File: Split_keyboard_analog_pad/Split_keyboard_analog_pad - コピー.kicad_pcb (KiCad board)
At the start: 2 copper layers, 313.3 x 128.7 mm, 162 parts, among them J1 Conn_01x05_Pin, J2 Conn_01x05_Pin, J3 Conn_01x08_Pin, J4 Conn_01x08_Pin, J5 Conn_01x02, J6 Conn_01x02, M2 MountingHole_2.2mm_M2, U1 nice_nano, U2 nice_nano

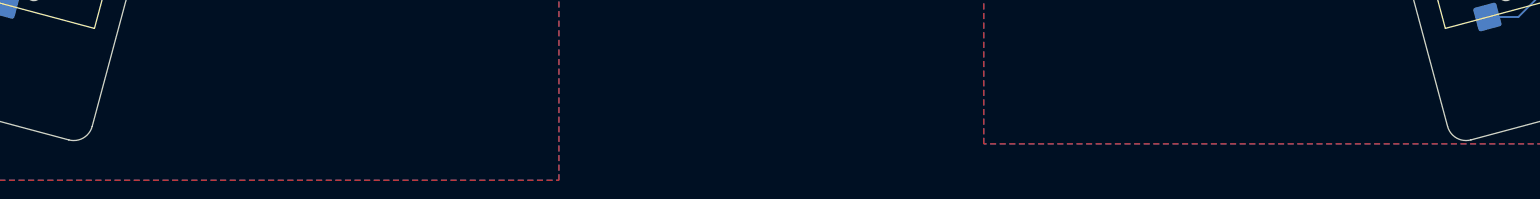
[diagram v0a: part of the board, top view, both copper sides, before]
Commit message: Add BT profile select hold tap
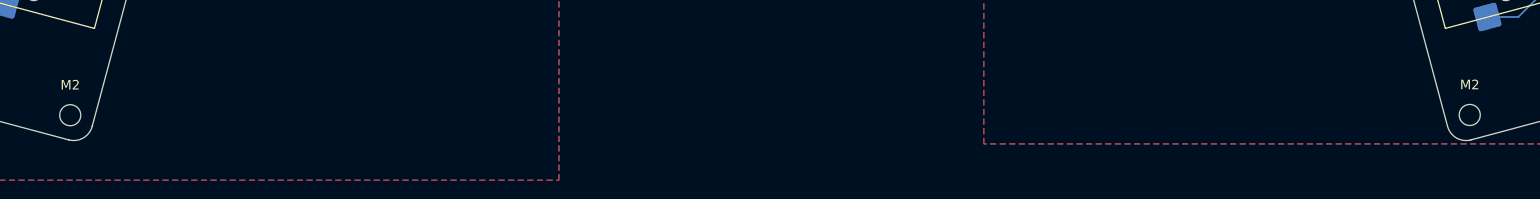
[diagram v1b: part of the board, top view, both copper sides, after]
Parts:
- added M2: MountingHole_2.2mm_M2, MountingHole:MountingHole_2.2mm_M2, F.Cu at (105.1, -44.9)
- added M2: MountingHole_2.2mm_M2, MountingHole:MountingHole_2.2mm_M2, F.Cu at (251.5, -44.9)
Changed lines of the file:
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@@
 	(net 118 "/RY_SUB")
 	(net 119 "Net-(D_L_4_7_SUB1-A)")
-	(net 120 "Net-(D_L_4_5-A)")
+	(net 120 "Net-(D_L_4_8_SUB1-A)")
 	(net 121 "/VCC_R_SUB")
 	(net 122 "/CL5_SUB")
 	(net 123 "/CL6_SUB")
 	(net 124 "Net-(D_L_4_2-A)")
-	(net 125 "Net-(D_L_4_8_SUB1-A)")
+	(net 125 "Net-(D_L_4_5-A)")
 	(net 126 "/CR0_SUB")
 	(net 127 "/CR1_SUB")
@@
 		(embedded_fonts no)
 	)
+	(footprint "MountingHole:MountingHole_2.2mm_M2"
+		(layer "F.Cu")
+		(at 105.0798 -44.9072)
+		(descr "Mounting Hole 2.2mm, M2, no annular, generated by kicad-footprint-generator mountinghole.py")
+		(tags "mountinghole M2")
+		(property "Reference" "M2"
+			(at 0 -3.15 0)
+			(layer "F.SilkS")
+			(effects
+				(font
+					(size 1 1)
+					(thickness 0.15)
+				)
+			)
+		)
+		(property "Value" "MountingHole_2.2mm_M2"
+			(at 0 3.15 0)
+			(layer "F.Fab")
+			(effects
+				(font
+					(size 1 1)
+					(thickness 0.15)
+				)
+			)
+		)
+		(property "Datasheet" ""
+			(at 0 0 0)
+			(layer "F.Fab")
+			(hide yes)
+			(effects
+				(font
+					(size 1.27 1.27)
+					(thickness 0.15)
+				)
+			)
+		)
+		(property "Description" ""
+			(at 0 0 0)
+			(layer "F.Fab")
+			(hide yes)
+			(effects
+				(font
+					(size 1.27 1.27)
+					(thickness 0.15)
+				)
+			)
+		)
+		(attr exclude_from_pos_files exclude_from_bom)
+		(fp_circle
+			(center 0 0)
+			(end 2.2 0)
+			(stroke
+				(width 0.15)
+				(type solid)
+			)
+			(fill no)
+			(layer "Cmts.User")
+		)
+		(fp_circle
+			(center 0 0)
+			(end 2.45 0)
+			(stroke
+				(width 0.05)
+				(type solid)
+			)
+			(fill no)
+			(layer "F.CrtYd")
+		)
+		(fp_text user "${REFERENCE}"
+			(at 0 0 0)
+			(layer "F.Fab")
+			(effects
+				(font
+					(size 1 1)
+					(thickness 0.15)
+				)
+			)
+		)
+		(pad "" np_thru_hole circle
+			(at 0 0)
+			(size 2.2 2.2)
+			(drill 2.2)
+			(layers "*.Cu" "*.Mask")
+		)
+		(embedded_fonts no)
+	)
 	(footprint "PCM_Switch_Keyboard_Kailh:SW_Kailh_Choc_V2_1.00u"
 		(layer "F.Cu")
@@
 			(layers "*.Cu" "*.Mask")
 			(remove_unused_layers no)
-			(net 120 "Net-(D_L_4_5-A)")
+			(net 125 "Net-(D_L_4_5-A)")
 			(pinfunction "1")
 			(pintype "passive")
@@
 			(layers "*.Cu" "*.Mask")
 			(remove_unused_layers no)
-			(net 125 "Net-(D_L_4_8_SUB1-A)")
+			(net 120 "Net-(D_L_4_8_SUB1-A)")
 			(pinfunction "1")
 			(pintype "passive")
@@
 	(footprint "MountingHole:MountingHole_2.2mm_M2"
 		(layer "F.Cu")
+		(at 251.5108 -44.9326)
+		(descr "Mounting Hole 2.2mm, M2, no annular, generated by kicad-footprint-generator mountinghole.py")
+		(tags "mountinghole M2")
+		(property "Reference" "M2"
+			(at 0 -3.15 0)
+			(layer "F.SilkS")
+			(effects
+				(font
+					(size 1 1)
+					(thickness 0.15)
+				)
+			)
+		)
+		(property "Value" "MountingHole_2.2mm_M2"
+			(at 0 3.15 0)
+			(layer "F.Fab")
+			(effects
+				(font
+					(size 1 1)
+					(thickness 0.15)
+				)
+			)
+		)
+		(property "Datasheet" ""
+			(at 0 0 0)
+			(layer "F.Fab")
+			(hide yes)
+			(effects
+				(font
+					(size 1.27 1.27)
+					(thickness 0.15)
+				)
+			)
+		)
+		(property "Description" ""
+			(at 0 0 0)
+			(layer "F.Fab")
+			(hide yes)
+			(effects
+				(font
+					(size 1.27 1.27)
+					(thickness 0.15)
+				)
+			)
+		)
+		(attr exclude_from_pos_files exclude_from_bom)
+		(fp_circle
+			(center 0 0)
+			(end 2.2 0)
+			(stroke
+				(width 0.15)
+				(type solid)
+			)
+			(fill no)
+			(layer "Cmts.User")
+		)
+		(fp_circle
+			(center 0 0)
+			(end 2.45 0)
+			(stroke
+				(width 0.05)
+				(type solid)
+			)
+			(fill no)
+			(layer "F.CrtYd")
+		)
+		(fp_text user "${REFERENCE}"
+			(at 0 0 0)
+			(layer "F.Fab")
+			(effects
+				(font
+					(size 1 1)
+					(thickness 0.15)
+				)
+			)
+		)
+		(pad "" np_thru_hole circle
+			(at 0 0)
+			(size 2.2 2.2)
+			(drill 2.2)
+			(layers "*.Cu" "*.Mask")
+		)
+		(embedded_fonts no)
+	)
+	(footprint "MountingHole:MountingHole_2.2mm_M2"
+		(layer "F.Cu")
 		(at 315.89035 -142.322798)
 		(descr "Mounting Hole 2.2mm, M2, no annular, generated by kicad-footprint-generator mountinghole.py")
@@
 			(layers "B.Cu" "B.Mask" "B.Paste")
 			(roundrect_rratio 0.25)
-			(net 125 "Net-(D_L_4_8_SUB1-A)")
+			(net 120 "Net-(D_L_4_8_SUB1-A)")
 			(pinfunction "A")
 			(pintype "passive")
@@
 			(layers "B.Cu" "B.Mask" "B.Paste")
 			(roundrect_rratio 0.25)
-			(net 120 "Net-(D_L_4_5-A)")
+			(net 125 "Net-(D_L_4_5-A)")
 			(pinfunction "A")
 			(pintype "passive")
@@
 	)
 	(segment
-		(start 164.1514 -103.814)
-		(end 163.3132 -102.9758)
+		(start 162.757 -120.804925)
+		(end 162.757 -144.884125)
 		(width 0.2)
 		(layer "B.Cu")
@@
 	)
 	(segment
-		(start 165.5814 -103.814)
-		(end 164.1514 -103.814)
+		(start 170.1278 -119.4666)
+		(end 164.095325 -119.4666)
 		(width 0.2)
 		(layer "B.Cu")
@@
 	)
 	(segment
-		(start 170.1278 -99.2676)
-		(end 165.5814 -103.814)
+		(start 166.889474 -149.016599)
+		(end 167.1778 -149.016599)
 		(width 0.2)
 		(layer "B.Cu")
@@
 	)
 	(segment
-		(start 163.3132 -88.6822)
-		(end 167.1778 -84.8176)
+		(start 162.757 -144.884125)
+		(end 166.889474 -149.016599)
 		(width 0.2)
 		(layer "B.Cu")
@@
 	)
 	(segment
-		(start 163.3132 -102.9758)
-		(end 163.3132 -88.6822)
+		(start 164.095325 -119.4666)
+		(end 162.757 -120.804925)
 		(width 0.2)
 		(layer "B.Cu")
@@
 	)
 	(segment
-		(start 162.757 -120.804925)
-		(end 162.757 -144.884125)
+		(start 164.1514 -103.814)
+		(end 163.3132 -102.9758)
 		(width 0.2)
 		(layer "B.Cu")
@@
 	)
 	(segment
-		(start 170.1278 -119.4666)
-		(end 164.095325 -119.4666)
+		(start 165.5814 -103.814)
+		(end 164.1514 -103.814)
 		(width 0.2)
 		(layer "B.Cu")
@@
 	)
 	(segment
-		(start 166.889474 -149.016599)
-		(end 167.1778 -149.016599)
+		(start 170.1278 -99.2676)
+		(end 165.5814 -103.814)
 		(width 0.2)
 		(layer "B.Cu")
@@
 	)
 	(segment
-		(start 162.757 -144.884125)
-		(end 166.889474 -149.016599)
+		(start 163.3132 -88.6822)
+		(end 167.1778 -84.8176)
 		(width 0.2)
 		(layer "B.Cu")
@@
 	)
 	(segment
-		(start 164.095325 -119.4666)
-		(end 162.757 -120.804925)
+		(start 163.3132 -102.9758)
+		(end 163.3132 -88.6822)
 		(width 0.2)
 		(layer "B.Cu")
